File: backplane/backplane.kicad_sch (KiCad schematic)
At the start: 2 parts, among them J2 Conn_01x10_Pin

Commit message: modified card edge connector
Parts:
- removed J1: ~, 2024-backplane:MR60PW-M_X3, symbol 2024-backplane:MR60PW-M_X3
- removed J2: Conn_01x10_Pin, 2024-backplane:CardEdge_2x10, symbol Connector:Conn_01x10_Pin
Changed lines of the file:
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@@
 (kicad_sch (version 20230121) (generator eeschema)
   (paper "A4")
-  (symbol (lib_id "2024-backplane:MR60PW-M_X3") (at 92.71 60.96 0) (unit 2)
-    (in_bom yes) (on_board yes) (dnp no) (fields_autoplaced)
-    (property "Reference" "J1" (at 96.52 54.61 0)
-      (effects (font (size 1.27 1.27)) (justify left))
-    )
-    (property "Value" "~" (at 88.9 54.61 0)
-      (effects (font (size 1.27 1.27)))
-    )
-    (property "Footprint" "2024-backplane:MR60PW-M_X3" (at 86.36 40.64 0)
-      (effects (font (size 1.27 1.27)) hide)
-    )
-    (property "Datasheet" "https://www.tme.com/Document/fd4b3517709a946d7b01cf4810656931/MR60PW-M.pdf" (at 87.63 43.18 0)
-      (effects (font (size 1.27 1.27)) hide)
-    )
-    (pin "2")
-    (pin "8")
-    (pin "5")
-    (pin "4")
-    (pin "7")
-    (pin "1")
-    (pin "6")
-    (pin "3")
-    (pin "9")
-    (instances
-      (project "backplane"
-        (path "/d02079f5-6f82-436e-968c-8505b701e298"
-          (reference "J1") (unit 2)
-        )
-      )
-    )
-  )
-  (symbol (lib_id "2024-backplane:MR60PW-M_X3") (at 73.66 60.96 0) (unit 1)
-    (in_bom yes) (on_board yes) (dnp no) (fields_autoplaced)
-    (property "Reference" "J1" (at 77.47 54.61 0)
-      (effects (font (size 1.27 1.27)) (justify left))
-    )
-    (property "Value" "~" (at 69.85 54.61 0)
-      (effects (font (size 1.27 1.27)))
-    )
-    (property "Footprint" "2024-backplane:MR60PW-M_X3" (at 67.31 40.64 0)
-      (effects (font (size 1.27 1.27)) hide)
-    )
-    (property "Datasheet" "https://www.tme.com/Document/fd4b3517709a946d7b01cf4810656931/MR60PW-M.pdf" (at 68.58 43.18 0)
-      (effects (font (size 1.27 1.27)) hide)
-    )
-    (pin "2")
-    (pin "8")
-    (pin "5")
-    (pin "4")
-    (pin "7")
-    (pin "1")
-    (pin "6")
-    (pin "3")
-    (pin "9")
-    (instances
-      (project "backplane"
-        (path "/d02079f5-6f82-436e-968c-8505b701e298"
-          (reference "J1") (unit 1)
-        )
-      )
-    )
-  )
-  (symbol (lib_id "2024-backplane:MR60PW-M_X3") (at 111.76 60.96 0) (unit 3)
-    (in_bom yes) (on_board yes) (dnp no) (fields_autoplaced)
-    (property "Reference" "J1" (at 115.57 54.61 0)
-      (effects (font (size 1.27 1.27)) (justify left))
-    )
-    (property "Value" "~" (at 107.95 54.61 0)
-      (effects (font (size 1.27 1.27)))
-    )
-    (property "Footprint" "2024-backplane:MR60PW-M_X3" (at 105.41 40.64 0)
-      (effects (font (size 1.27 1.27)) hide)
-    )
-    (property "Datasheet" "https://www.tme.com/Document/fd4b3517709a946d7b01cf4810656931/MR60PW-M.pdf" (at 106.68 43.18 0)
-      (effects (font (size 1.27 1.27)) hide)
-    )
-    (pin "2")
-    (pin "8")
-    (pin "5")
-    (pin "4")
-    (pin "7")
-    (pin "1")
-    (pin "6")
-    (pin "3")
-    (pin "9")
-    (instances
-      (project "backplane"
-        (path "/d02079f5-6f82-436e-968c-8505b701e298"
-          (reference "J1") (unit 3)
-        )
-      )
-    )
-  )
-  (symbol (lib_id "Connector:Conn_01x10_Pin") (at 125.73 85.09 90) (unit 1)
-    (in_bom yes) (on_board yes) (dnp no) (fields_autoplaced)
-    (property "Reference" "J2" (at 127 87.63 90)
-      (effects (font (size 1.27 1.27)))
-    )
-    (property "Value" "Conn_01x10_Pin" (at 127 90.17 90)
-      (effects (font (size 1.27 1.27)))
-    )
-    (property "Footprint" "2024-backplane:CardEdge_2x10" (at 125.73 85.09 0)
-      (effects (font (size 1.27 1.27)) hide)
-    )
-    (property "Datasheet" "~" (at 125.73 85.09 0)
-      (effects (font (size 1.27 1.27)) hide)
-    )
-    (pin "10")
-    (pin "4")
-    (pin "2")
-    (pin "1")
-    (pin "6")
-    (pin "8")
-    (pin "3")
-    (pin "7")
-    (pin "9")
-    (pin "5")
-    (instances
-      (project "backplane"
-        (path "/d02079f5-6f82-436e-968c-8505b701e298"
-          (reference "J2") (unit 1)
-        )
-      )
-    )
-  )
   (sheet_instances
     (path "/" (page "1"))

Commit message: duplicate xt90 connector footprint with nums
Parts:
- added J1: Conn_01x10, 2024-backplane:EDAC_Edge_2x10, symbol Connector_Generic:Conn_01x10
- added J2: ~, 2024-backplane:MR60PW-M_X3, symbol 2024-backplane:MR60PW-M_X3
- added J3, J4: 48V in, symbol Connector_Generic:Conn_01x02
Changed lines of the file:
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@@
 (kicad_sch (version 20230121) (generator eeschema)
   (paper "A4")
+  (symbol (lib_id "2024-backplane:MR60PW-M_X3") (at 88.9 59.69 270) (unit 2)
+    (in_bom yes) (on_board yes) (dnp no) (fields_autoplaced)
+    (property "Reference" "J2" (at 100.33 55.88 90)
+      (effects (font (size 1.27 1.27)) (justify left))
+    )
+    (property "Value" "~" (at 95.25 55.88 0)
+      (effects (font (size 1.27 1.27)))
+    )
+    (property "Footprint" "2024-backplane:MR60PW-M_X3" (at 109.22 53.34 0)
+      (effects (font (size 1.27 1.27)) hide)
+    )
+    (property "Datasheet" "https://www.tme.com/Document/fd4b3517709a946d7b01cf4810656931/MR60PW-M.pdf" (at 106.68 54.61 0)
+      (effects (font (size 1.27 1.27)) hide)
+    )
+    (pin "9")
+    (pin "8")
+    (pin "7")
+    (pin "4")
+    (pin "5")
+    (pin "6")
+    (pin "3")
+    (pin "2")
+    (pin "1")
+    (instances
+      (project "backplane"
+        (path "/d02079f5-6f82-436e-968c-8505b701e298"
+          (reference "J2") (unit 2)
+        )
+      )
+    )
+  )
+  (symbol (lib_id "Connector_Generic:Conn_01x02") (at 36.83 68.58 180) (unit 1)
+    (in_bom yes) (on_board yes) (dnp no) (fields_autoplaced)
+    (property "Reference" "J3" (at 36.83 59.69 0)
+      (effects (font (size 1.27 1.27)))
+    )
+    (property "Value" "48V in" (at 36.83 62.23 0)
+      (effects (font (size 1.27 1.27)))
+    )
+    (property "Footprint" "" (at 36.83 68.58 0)
+      (effects (font (size 1.27 1.27)) hide)
+    )
+    (property "Datasheet" "~" (at 36.83 68.58 0)
+      (effects (font (size 1.27 1.27)) hide)
+    )
+    (pin "2")
+    (pin "1")
+    (instances
+      (project "backplane"
+        (path "/d02079f5-6f82-436e-968c-8505b701e298"
+          (reference "J3") (unit 1)
+        )
+      )
+    )
+  )
+  (symbol (lib_id "Connector_Generic:Conn_01x10") (at 93.98 90.17 0) (unit 1)
+    (in_bom yes) (on_board yes) (dnp no)
+    (property "Reference" "J1" (at 93.98 109.22 0)
+      (effects (font (size 1.27 1.27)))
+    )
+    (property "Value" "Conn_01x10" (at 93.98 106.68 0)
+      (effects (font (size 1.27 1.27)))
+    )
+    (property "Footprint" "2024-backplane:EDAC_Edge_2x10" (at 93.98 90.17 0)
+      (effects (font (size 1.27 1.27)) hide)
+    )
+    (property "Datasheet" "~" (at 93.98 90.17 0)
+      (effects (font (size 1.27 1.27)) hide)
+    )
+    (pin "6")
+    (pin "10")
+    (pin "1")
+    (pin "3")
+    (pin "4")
+    (pin "8")
+    (pin "7")
+    (pin "2")
+    (pin "5")
+    (pin "9")
+    (instances
+      (project "backplane"
+        (path "/d02079f5-6f82-436e-968c-8505b701e298"
+          (reference "J1") (unit 1)
+        )
+      )
+    )
+  )
+  (symbol (lib_id "2024-backplane:MR60PW-M_X3") (at 88.9 45.72 270) (unit 1)
+    (in_bom yes) (on_board yes) (dnp no) (fields_autoplaced)
+    (property "Reference" "J2" (at 100.33 41.91 90)
+      (effects (font (size 1.27 1.27)) (justify left))
+    )
+    (property "Value" "~" (at 95.25 41.91 0)
+      (effects (font (size 1.27 1.27)))
+    )
+    (property "Footprint" "2024-backplane:MR60PW-M_X3" (at 109.22 39.37 0)
+      (effects (font (size 1.27 1.27)) hide)
+    )
+    (property "Datasheet" "https://www.tme.com/Document/fd4b3517709a946d7b01cf4810656931/MR60PW-M.pdf" (at 106.68 40.64 0)
+      (effects (font (size 1.27 1.27)) hide)
+    )
+    (pin "9")
+    (pin "8")
+    (pin "7")
+    (pin "4")
+    (pin "5")
+    (pin "6")
+    (pin "3")
+    (pin "2")
+    (pin "1")
+    (instances
+      (project "backplane"
+        (path "/d02079f5-6f82-436e-968c-8505b701e298"
+          (reference "J2") (unit 1)
+        )
+      )
+    )
+  )
+  (symbol (lib_id "power:GND1") (at 46.99 88.9 0) (unit 1)
+    (in_bom yes) (on_board yes) (dnp no) (fields_autoplaced)
+    (property "Reference" "#PWR01" (at 46.99 95.25 0)
+      (effects (font (size 1.27 1.27)) hide)
+    )
+    (property "Value" "GND1" (at 46.99 93.98 0)
+      (effects (font (size 1.27 1.27)))
+    )
+    (property "Footprint" "" (at 46.99 88.9 0)
+      (effects (font (size 1.27 1.27)) hide)
+    )
+    (property "Datasheet" "" (at 46.99 88.9 0)
+      (effects (font (size 1.27 1.27)) hide)
+    )
+    (pin "1")
+    (instances
+      (project "backplane"
+        (path "/d02079f5-6f82-436e-968c-8505b701e298"
+          (reference "#PWR01") (unit 1)
+        )
+      )
+    )
+  )
+  (symbol (lib_id "Connector_Generic:Conn_01x02") (at 36.83 83.82 180) (unit 1)
+    (in_bom yes) (on_board yes) (dnp no) (fields_autoplaced)
+    (property "Reference" "J4" (at 36.83 74.93 0)
+      (effects (font (size 1.27 1.27)))
+    )
+    (property "Value" "48V in" (at 36.83 77.47 0)
+      (effects (font (size 1.27 1.27)))
+    )
+    (property "Footprint" "" (at 36.83 83.82 0)
+      (effects (font (size 1.27 1.27)) hide)
+    )
+    (property "Datasheet" "~" (at 36.83 83.82 0)
+      (effects (font (size 1.27 1.27)) hide)
+    )
+    (pin "2")
+    (pin "1")
+    (instances
+      (project "backplane"
+        (path "/d02079f5-6f82-436e-968c-8505b701e298"
+          (reference "J4") (unit 1)
+        )
+      )
+    )
+  )
+  (symbol (lib_id "2024-backplane:MR60PW-M_X3") (at 88.9 73.66 270) (unit 3)
+    (in_bom yes) (on_board yes) (dnp no) (fields_autoplaced)
+    (property "Reference" "J2" (at 100.33 69.85 90)
+      (effects (font (size 1.27 1.27)) (justify left))
+    )
+    (property "Value" "~" (at 95.25 69.85 0)
+      (effects (font (size 1.27 1.27)))
+    )
+    (property "Footprint" "2024-backplane:MR60PW-M_X3" (at 109.22 67.31 0)
+      (effects (font (size 1.27 1.27)) hide)
+    )
+    (property "Datasheet" "https://www.tme.com/Document/fd4b3517709a946d7b01cf4810656931/MR60PW-M.pdf" (at 106.68 68.58 0)
+      (effects (font (size 1.27 1.27)) hide)
+    )
+    (pin "9")
+    (pin "8")
+    (pin "7")
+    (pin "4")
+    (pin "5")
+    (pin "6")
+    (pin "3")
+    (pin "2")
+    (pin "1")
+    (instances
+      (project "backplane"
+        (path "/d02079f5-6f82-436e-968c-8505b701e298"
+          (reference "J2") (unit 3)
+        )
+      )
+    )
+  )
   (sheet_instances
     (path "/" (page "1"))

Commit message: backplane schematic
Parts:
- added J10, J12, J14, J16, J18, J20, J6, J8: Conn_01x10, 2024-backplane:EDAC_Edge_2x10, symbol Connector_Generic:Conn_01x10
- added J11, J13, J15, J17, J19, J5, J7, J9: ~, 2024-backplane:MR60PW-M_X3, symbol 2024-backplane:MR60PW-M_X3
- J3, J4: footprint (none) -> 2024-backplane:AMASS_XT90PW-M_MOD_NUMS
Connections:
- net GND1: now also J2.2 (GND), J2.3 (GND), J2.8 (GND), J3.2 (Pin_2), J4.2 (Pin_2), J11.2 (GND), J11.3 (GND), J11.8 (GND), J13.2 (GND), J13.3 (GND), J13.8 (GND), J15.2 (GND), J15.3 (GND), J15.8 (GND), J17.2 (GND), J17.3 (GND), J17.8 (GND), J19.2 (GND), J19.3 (GND), J19.8 (GND), J5.2 (GND), J5.3 (GND), J5.8 (GND), J7.2 (GND), J7.3 (GND), J7.8 (GND), J9.2 (GND), J9.3 (GND), J9.8 (GND)
- net 12v_1: now reaches J2.4 (12V)
- net 12v_1: now also J11.4 (12V), J13.4 (12V), J15.4 (12V), J17.4 (12V), J19.4 (12V), J5.4 (12V), J7.4 (12V), J9.4 (12V)
- net 12v_2: now reaches J2.5 (12V)
- net 12v_2: now also J11.5 (12V), J13.5 (12V), J15.5 (12V), J17.5 (12V), J19.5 (12V), J5.5 (12V), J7.5 (12V), J9.5 (12V)
- net 12v_3: now reaches J2.6 (12V)
- net 12v_3: now also J11.6 (12V), J13.6 (12V), J15.6 (12V), J17.6 (12V), J19.6 (12V), J5.6 (12V), J7.6 (12V), J9.6 (12V)
- net 48v: now reaches J3.1 (Pin_1)
- net 48v: now also J2.1 (48V), J4.1 (Pin_1), J11.1 (48V), J13.1 (48V), J15.1 (48V), J17.1 (48V), J19.1 (48V), J5.1 (48V), J7.1 (48V), J9.1 (48V)
- net a: now reaches J1.1 (Pin_1)
- net a: now also J10.1 (Pin_1), J12.1 (Pin_1), J14.1 (Pin_1), J16.1 (Pin_1), J18.1 (Pin_1), J20.1 (Pin_1), J6.1 (Pin_1), J8.1 (Pin_1)
- net j: now reaches J1.10 (Pin_10)
- net j: now also J10.10 (Pin_10), J12.10 (Pin_10), J14.10 (Pin_10), J16.10 (Pin_10), J18.10 (Pin_10), J20.10 (Pin_10), J6.10 (Pin_10), J8.10 (Pin_10)
- net b: now reaches J1.2 (Pin_2)
- net b: now also J10.2 (Pin_2), J12.2 (Pin_2), J14.2 (Pin_2), J16.2 (Pin_2), J18.2 (Pin_2), J20.2 (Pin_2), J6.2 (Pin_2), J8.2 (Pin_2)
- net c: now reaches J1.3 (Pin_3)
- net c: now also J10.3 (Pin_3), J12.3 (Pin_3), J14.3 (Pin_3), J16.3 (Pin_3), J18.3 (Pin_3), J20.3 (Pin_3), J6.3 (Pin_3), J8.3 (Pin_3)
- net d: now reaches J1.4 (Pin_4)
- net d: now also J10.4 (Pin_4), J12.4 (Pin_4), J14.4 (Pin_4), J16.4 (Pin_4), J18.4 (Pin_4), J20.4 (Pin_4), J6.4 (Pin_4), J8.4 (Pin_4)
- net e: now reaches J1.5 (Pin_5)
- net e: now also J10.5 (Pin_5), J12.5 (Pin_5), J14.5 (Pin_5), J16.5 (Pin_5), J18.5 (Pin_5), J20.5 (Pin_5), J6.5 (Pin_5), J8.5 (Pin_5)
- net f: now reaches J1.6 (Pin_6)
- net f: now also J10.6 (Pin_6), J12.6 (Pin_6), J14.6 (Pin_6), J16.6 (Pin_6), J18.6 (Pin_6), J20.6 (Pin_6), J6.6 (Pin_6), J8.6 (Pin_6)
- net g: now reaches J1.7 (Pin_7)
- net g: now also J10.7 (Pin_7), J12.7 (Pin_7), J14.7 (Pin_7), J16.7 (Pin_7), J18.7 (Pin_7), J20.7 (Pin_7), J6.7 (Pin_7), J8.7 (Pin_7)
- net h: now reaches J1.8 (Pin_8)
- net h: now also J10.8 (Pin_8), J12.8 (Pin_8), J14.8 (Pin_8), J16.8 (Pin_8), J18.8 (Pin_8), J20.8 (Pin_8), J6.8 (Pin_8), J8.8 (Pin_8)
- net i: now reaches J1.9 (Pin_9)
- net i: now also J10.9 (Pin_9), J12.9 (Pin_9), J14.9 (Pin_9), J16.9 (Pin_9), J18.9 (Pin_9), J20.9 (Pin_9), J6.9 (Pin_9), J8.9 (Pin_9)
- net 24v: now reaches J2.7 (24V)
- net 24v: now also J11.7 (24V), J13.7 (24V), J15.7 (24V), J17.7 (24V), J19.7 (24V), J5.7 (24V), J7.7 (24V), J9.7 (24V)
- net 5v: now reaches J2.9 (5V)
- net 5v: now also J11.9 (5V), J13.9 (5V), J15.9 (5V), J17.9 (5V), J19.9 (5V), J5.9 (5V), J7.9 (5V), J9.9 (5V)
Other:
- note added: "ESC 1"
- note added: "ESC 2"
- note added: "ESC 3"
- note added: "MAIN BOARD"
- note added: "POW 1"
- note added: "POW 2"
- note added: "POW 3"
- note added: "POW 4"
- note added: "POW 5"
- moved on the sheet: J1, J2A, J2B, J2C, J3

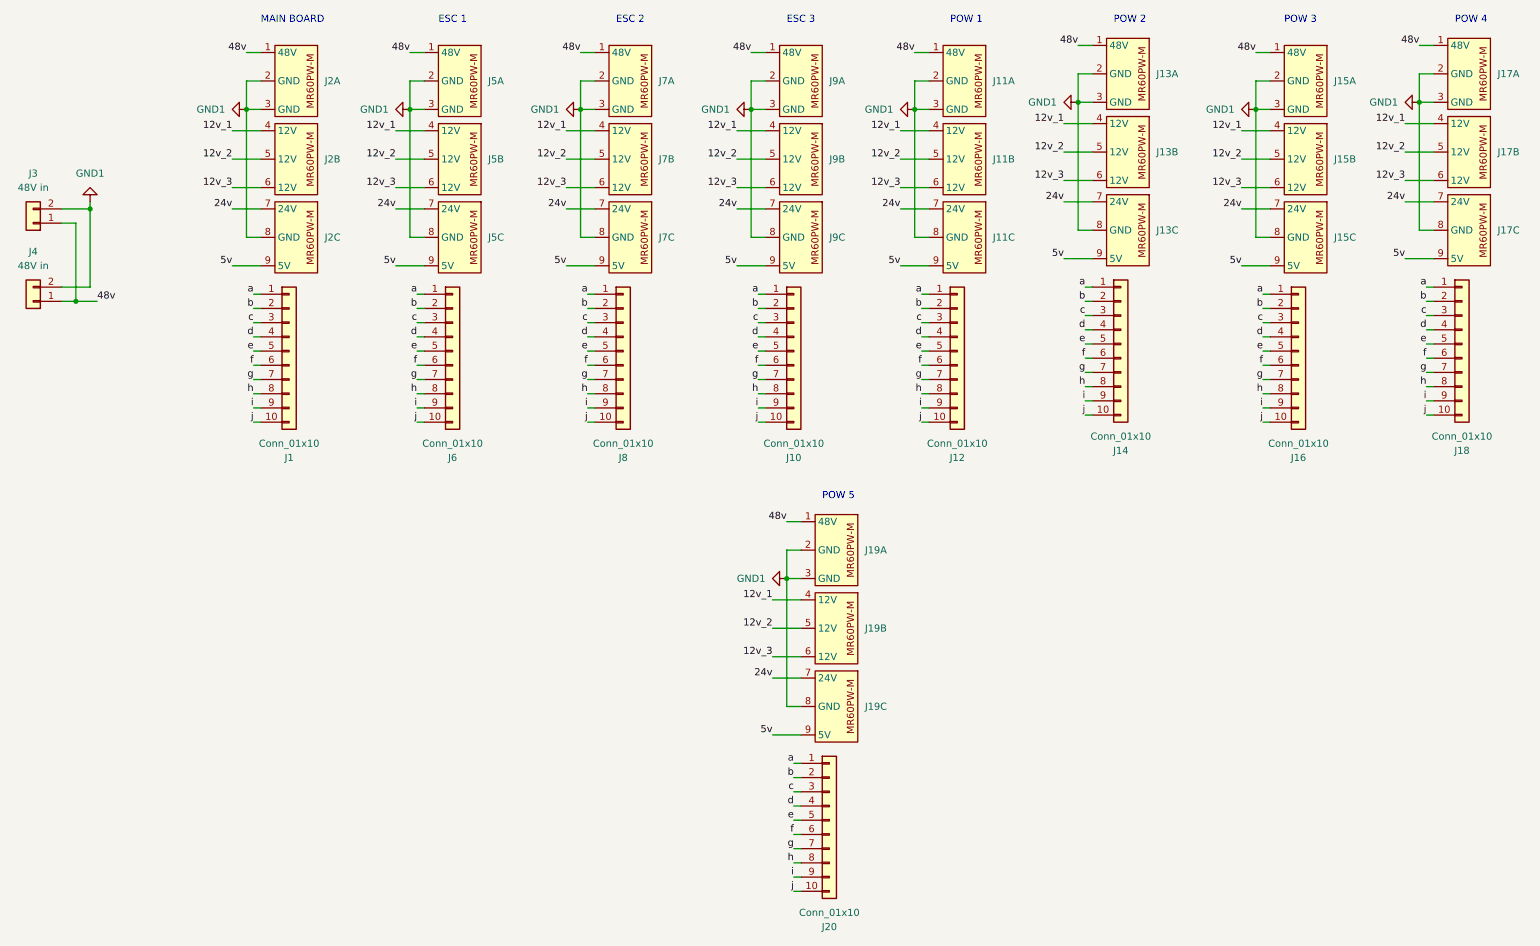
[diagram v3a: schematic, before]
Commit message: finalized backplane schematic, started pcb layout
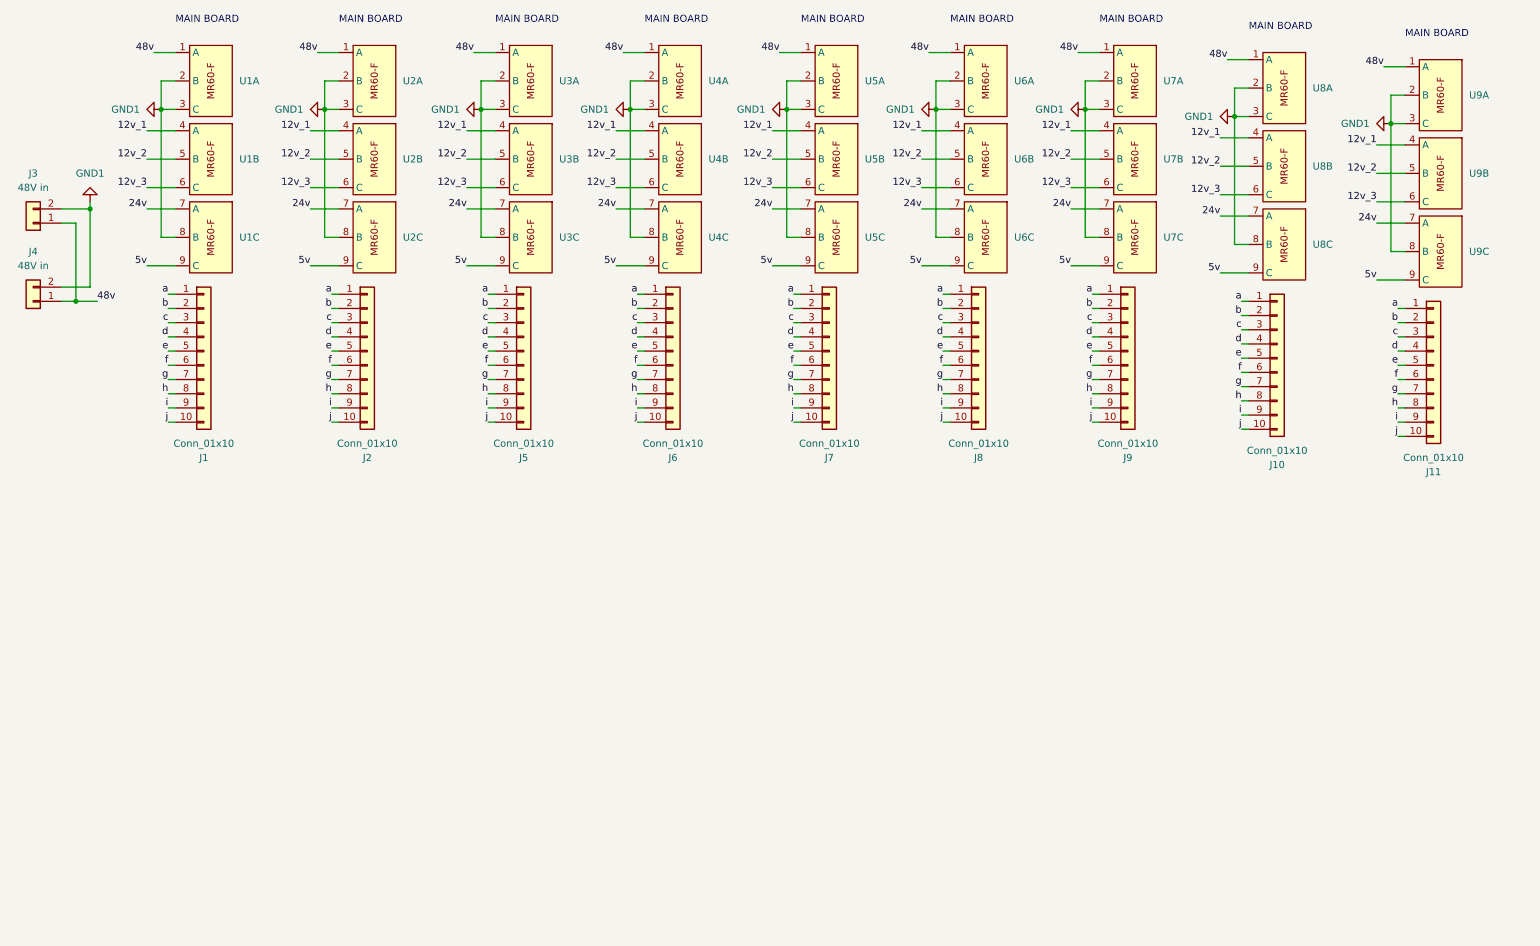
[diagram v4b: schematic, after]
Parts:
- removed J11, J13, J15, J17, J19, J2, J5, J7, J9: ~, 2024-backplane:MR60PW-M_X3, symbol 2024-backplane:MR60PW-M_X3
- removed J12, J14, J16, J18, J20: Conn_01x10, 2024-backplane:EDAC_Edge_2x10, symbol Connector_Generic:Conn_01x10
- added J11, J2, J5, J7, J9: Conn_01x10, 2024-backplane:EDAC_Edge_2x10, symbol Connector_Generic:Conn_01x10
- added U1, U2, U3, U4, U5, U6, U7, U8, U9: ~, 2024-backplane:MR60-F_X3, symbol 2024-backplane:MR60-F_X3
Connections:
- net 12v_1: now also U1.4 (A), U2.4 (A), U3.4 (A), U4.4 (A), U5.4 (A), U6.4 (A), U7.4 (A), U8.4 (A), U9.4 (A)
- net 12v_2: now also U1.5 (B), U2.5 (B), U3.5 (B), U4.5 (B), U5.5 (B), U6.5 (B), U7.5 (B), U8.5 (B), U9.5 (B)
- net 12v_3: now also U1.6 (C), U2.6 (C), U3.6 (C), U4.6 (C), U5.6 (C), U6.6 (C), U7.6 (C), U8.6 (C), U9.6 (C)
- net 24v: now also U1.7 (A), U2.7 (A), U3.7 (A), U4.7 (A), U5.7 (A), U6.7 (A), U7.7 (A), U8.7 (A), U9.7 (A)
- net 48v: now also U1.1 (A), U2.1 (A), U3.1 (A), U4.1 (A), U5.1 (A), U6.1 (A), U7.1 (A), U8.1 (A), U9.1 (A)
- net 5v: now also U1.9 (C), U2.9 (C), U3.9 (C), U4.9 (C), U5.9 (C), U6.9 (C), U7.9 (C), U8.9 (C), U9.9 (C)
- net GND1: now also U1.2 (B), U1.3 (C), U1.8 (B), U2.2 (B), U2.3 (C), U2.8 (B), U3.2 (B), U3.3 (C), U3.8 (B), U4.2 (B), U4.3 (C), U4.8 (B), U5.2 (B), U5.3 (C), U5.8 (B), U6.2 (B), U6.3 (C), U6.8 (B), U7.2 (B), U7.3 (C), U7.8 (B), U8.2 (B), U8.3 (C), U8.8 (B), U9.2 (B), U9.3 (C), U9.8 (B)
- net a: now also J11.1 (Pin_1), J2.1 (Pin_1), J5.1 (Pin_1), J7.1 (Pin_1), J9.1 (Pin_1)
- net b: now also J11.2 (Pin_2), J2.2 (Pin_2), J5.2 (Pin_2), J7.2 (Pin_2), J9.2 (Pin_2)
- net c: now also J11.3 (Pin_3), J2.3 (Pin_3), J5.3 (Pin_3), J7.3 (Pin_3), J9.3 (Pin_3)
- net d: now also J11.4 (Pin_4), J2.4 (Pin_4), J5.4 (Pin_4), J7.4 (Pin_4), J9.4 (Pin_4)
- net e: now also J11.5 (Pin_5), J2.5 (Pin_5), J5.5 (Pin_5), J7.5 (Pin_5), J9.5 (Pin_5)
- net f: now also J11.6 (Pin_6), J2.6 (Pin_6), J5.6 (Pin_6), J7.6 (Pin_6), J9.6 (Pin_6)
- net g: now also J11.7 (Pin_7), J2.7 (Pin_7), J5.7 (Pin_7), J7.7 (Pin_7), J9.7 (Pin_7)
- net h: now also J11.8 (Pin_8), J2.8 (Pin_8), J5.8 (Pin_8), J7.8 (Pin_8), J9.8 (Pin_8)
- net i: now also J11.9 (Pin_9), J2.9 (Pin_9), J5.9 (Pin_9), J7.9 (Pin_9), J9.9 (Pin_9)
- net j: now also J11.10 (Pin_10), J2.10 (Pin_10), J5.10 (Pin_10), J7.10 (Pin_10), J9.10 (Pin_10)
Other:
- note removed: "ESC 1"
- note removed: "ESC 2"
- note removed: "ESC 3"
- note removed: "POW 1"
- note removed: "POW 2"
- note removed: "POW 3"
- note removed: "POW 4"
- note removed: "POW 5"
- moved on the sheet: J1
